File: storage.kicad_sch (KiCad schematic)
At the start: 26 parts, among them J11 uSD card, J9 uSD card, P1 uBUS1, P2 uBUS2, Q1 BC856, Q3 BC856, U19 IS61WV20488BLL-10TLI, U20 IS61WV20488BLL-10TLI, U21 MT48LC16M16A2TG

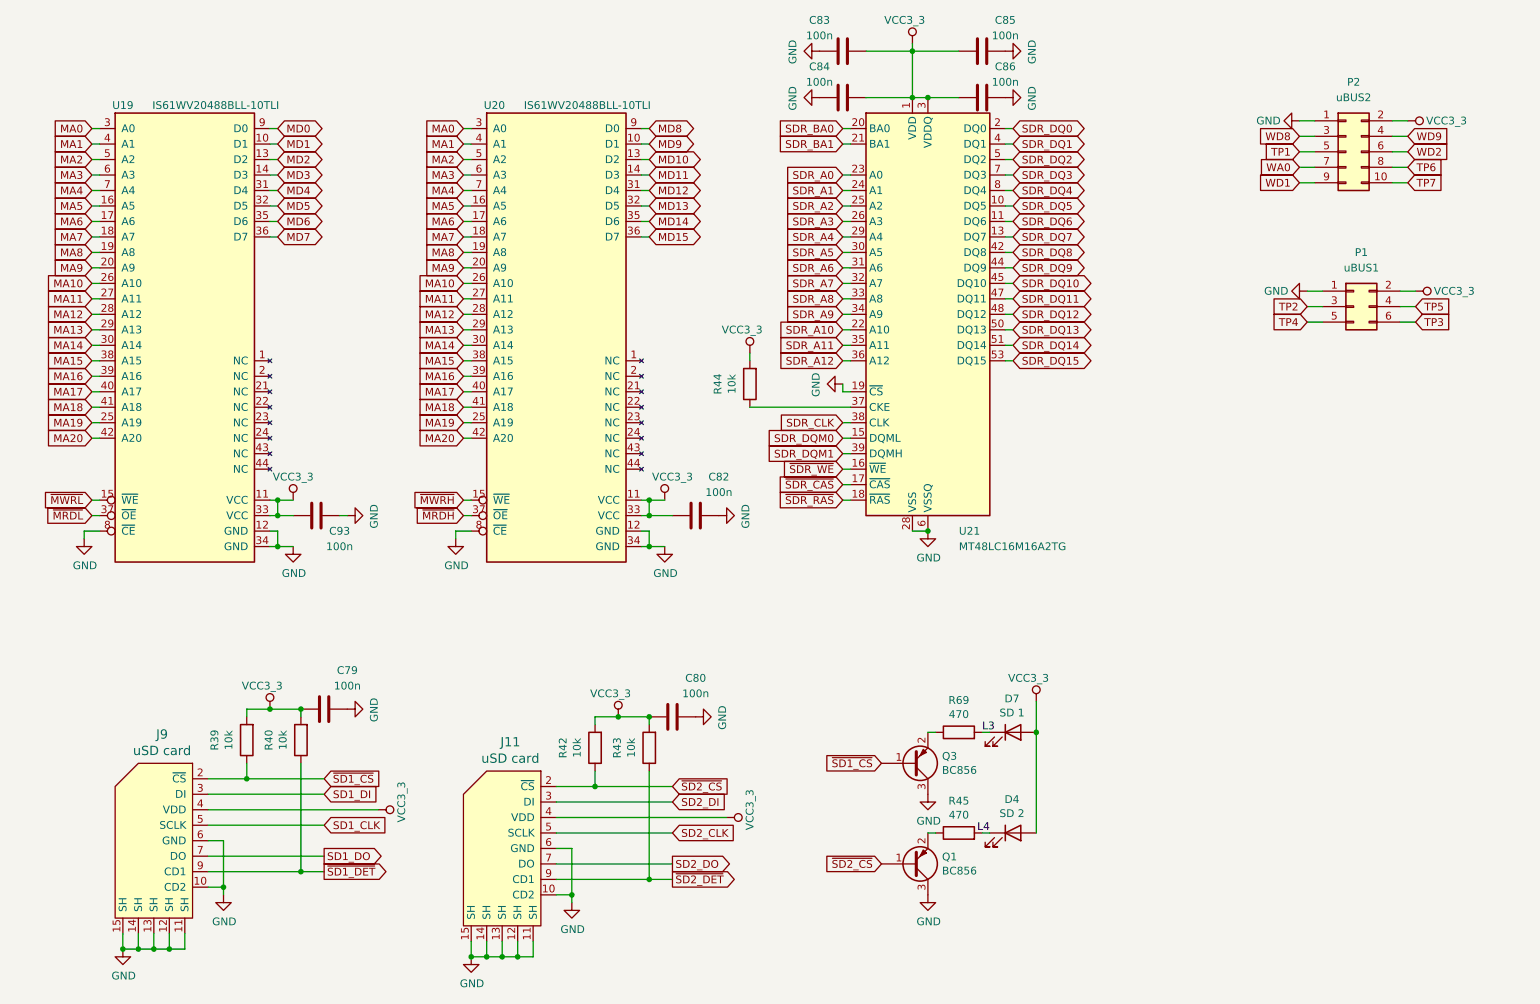
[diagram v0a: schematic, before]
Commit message: Updated revA: replaced resistors with IC for HDMI protection
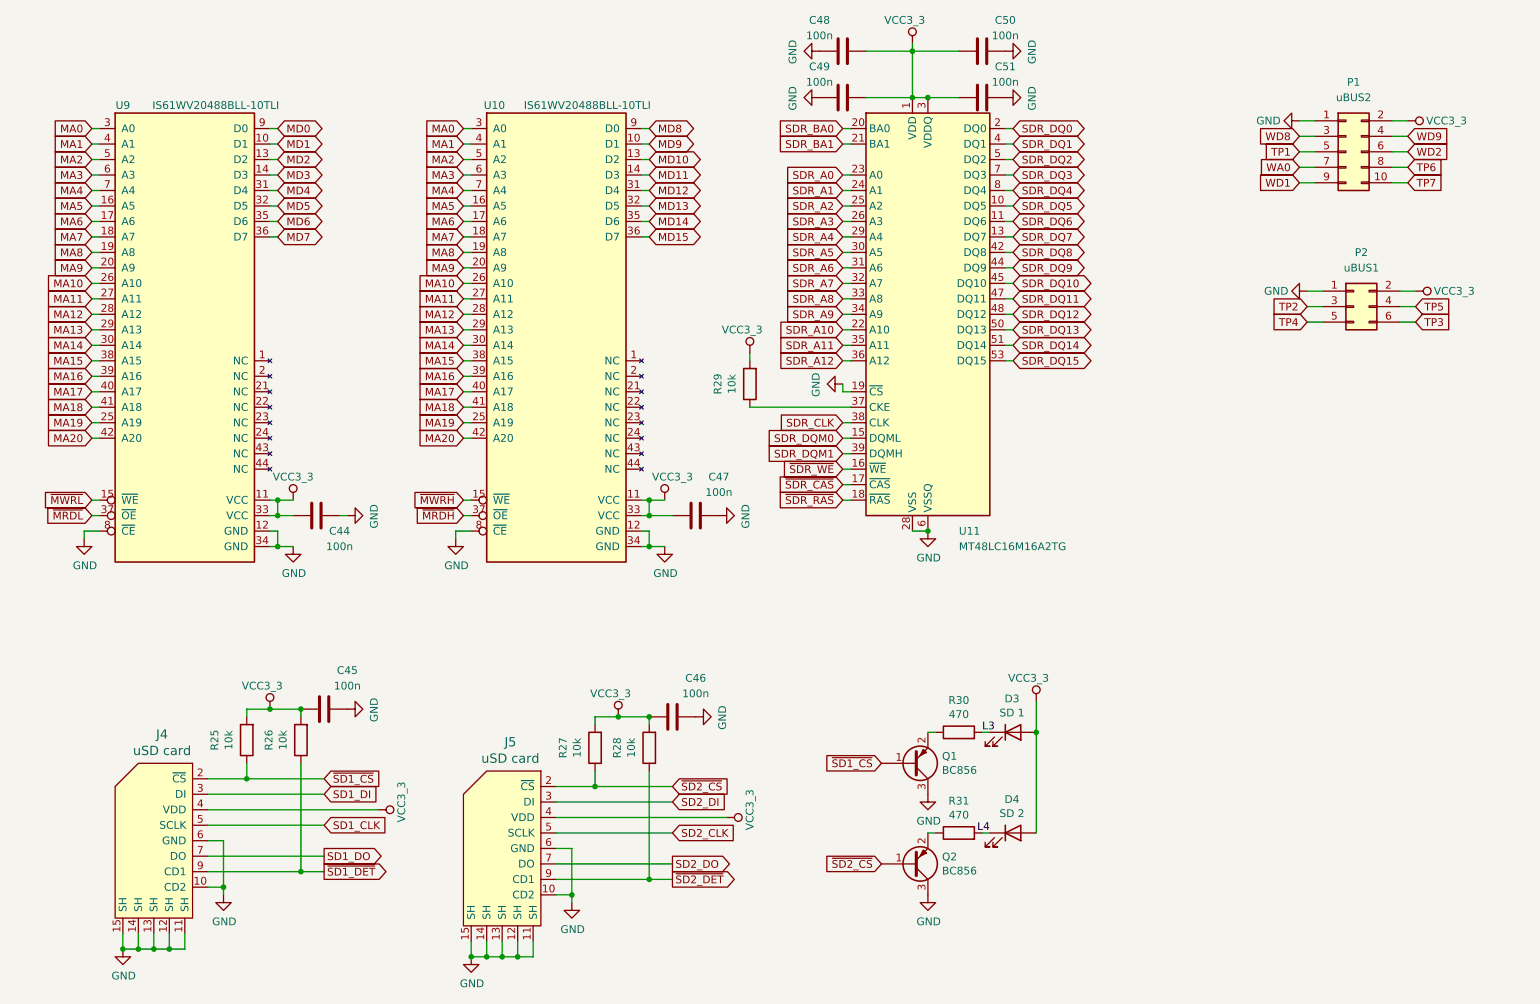
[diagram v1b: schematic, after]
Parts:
- renumbered C93 to C44, C79 to C45, C80 to C46, C82 to C47, C83 to C48, C84 to C49, C85 to C50, C86 to C51, D7 to D3, J9 to J4, J11 to J5, P2 to P1, P1 to P2, Q3 to Q1, Q1 to Q2, R39 to R25, R40 to R26, R42 to R27, R43 to R28, R44 to R29, R69 to R30, R45 to R31, U20 to U10, U21 to U11, U19 to U9

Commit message: Cleanup revA
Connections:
- net TP1 renamed UBUS_6
- net TP2 renamed UBUS_0
- net TP3 renamed UBUS_3
- net TP4 renamed UBUS_2
- net TP5 renamed UBUS_1
- net TP6 renamed UBUS_9
- net TP7 renamed UBUS_11
- net WA0 renamed UBUS_8
- net WD1 renamed UBUS_10
- net WD2 renamed UBUS_7
- net WD8 renamed UBUS_4
- net WD9 renamed UBUS_5
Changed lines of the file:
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@@
     (effects (font (size 1.27 1.27)) (justify left bottom))
   )
-  (global_label "TP7" (shape input) (at 242.57 44.45 0) (fields_autoplaced)
-    (effects (font (size 1.27 1.27)) (justify left))
-    (property "Intersheetrefs" "${INTERSHEET_REFS}" (at 249.0023 44.45 0)
+  (global_label "UBUS_11" (shape input) (at 242.57 44.45 0) (fields_autoplaced)
+    (effects (font (size 1.27 1.27)) (justify left))
+    (property "Intersheetrefs" "${INTERSHEET_REFS}" (at 254.0823 44.45 0)
       (effects (font (size 1.27 1.27)) (justify left) hide)
     )
@@
     )
   )
-  (global_label "TP4" (shape input) (at 226.06 67.31 180) (fields_autoplaced)
-    (effects (font (size 1.27 1.27)) (justify right))
-    (property "Intersheetrefs" "${INTERSHEET_REFS}" (at 219.6277 67.31 0)
+  (global_label "UBUS_2" (shape input) (at 226.06 67.31 180) (fields_autoplaced)
+    (effects (font (size 1.27 1.27)) (justify right))
+    (property "Intersheetrefs" "${INTERSHEET_REFS}" (at 215.7572 67.31 0)
       (effects (font (size 1.27 1.27)) (justify right) hide)
     )
@@
     )
   )
-  (global_label "TP2" (shape input) (at 226.06 64.77 180) (fields_autoplaced)
-    (effects (font (size 1.27 1.27)) (justify right))
-    (property "Intersheetrefs" "${INTERSHEET_REFS}" (at 219.6277 64.77 0)
+  (global_label "UBUS_0" (shape input) (at 226.06 64.77 180) (fields_autoplaced)
+    (effects (font (size 1.27 1.27)) (justify right))
+    (property "Intersheetrefs" "${INTERSHEET_REFS}" (at 215.7572 64.77 0)
       (effects (font (size 1.27 1.27)) (justify right) hide)
     )
@@
     )
   )
-  (global_label "TP1" (shape input) (at 224.79 39.37 180) (fields_autoplaced)
-    (effects (font (size 1.27 1.27)) (justify right))
-    (property "Intersheetrefs" "${INTERSHEET_REFS}" (at 218.3577 39.37 0)
-      (effects (font (size 1.27 1.27)) (justify right) hide)
-    )
-  )
-  (global_label "TP6" (shape input) (at 242.57 41.91 0) (fields_autoplaced)
-    (effects (font (size 1.27 1.27)) (justify left))
-    (property "Intersheetrefs" "${INTERSHEET_REFS}" (at 249.0023 41.91 0)
+  (global_label "UBUS_6" (shape input) (at 224.79 39.37 180) (fields_autoplaced)
+    (effects (font (size 1.27 1.27)) (justify right))
+    (property "Intersheetrefs" "${INTERSHEET_REFS}" (at 214.4872 39.37 0)
+      (effects (font (size 1.27 1.27)) (justify right) hide)
+    )
+  )
+  (global_label "UBUS_9" (shape input) (at 242.57 41.91 0) (fields_autoplaced)
+    (effects (font (size 1.27 1.27)) (justify left))
+    (property "Intersheetrefs" "${INTERSHEET_REFS}" (at 252.8728 41.91 0)
       (effects (font (size 1.27 1.27)) (justify left) hide)
     )
@@
     )
   )
-  (global_label "WD8" (shape input) (at 224.79 36.83 180) (fields_autoplaced)
-    (effects (font (size 1.27 1.27)) (justify right))
-    (property "Intersheetrefs" "${INTERSHEET_REFS}" (at 217.8739 36.83 0)
+  (global_label "UBUS_4" (shape input) (at 224.79 36.83 180) (fields_autoplaced)
+    (effects (font (size 1.27 1.27)) (justify right))
+    (property "Intersheetrefs" "${INTERSHEET_REFS}" (at 214.4872 36.83 0)
       (effects (font (size 1.27 1.27)) (justify right) hide)
     )
@@
     )
   )
-  (global_label "WD9" (shape input) (at 242.57 36.83 0) (fields_autoplaced)
-    (effects (font (size 1.27 1.27)) (justify left))
-    (property "Intersheetrefs" "${INTERSHEET_REFS}" (at 249.4861 36.83 0)
+  (global_label "UBUS_5" (shape input) (at 242.57 36.83 0) (fields_autoplaced)
+    (effects (font (size 1.27 1.27)) (justify left))
+    (property "Intersheetrefs" "${INTERSHEET_REFS}" (at 252.8728 36.83 0)
       (effects (font (size 1.27 1.27)) (justify left) hide)
     )
@@
     )
   )
-  (global_label "WD1" (shape input) (at 224.79 44.45 180) (fields_autoplaced)
-    (effects (font (size 1.27 1.27)) (justify right))
-    (property "Intersheetrefs" "${INTERSHEET_REFS}" (at 217.8739 44.45 0)
+  (global_label "UBUS_10" (shape input) (at 224.79 44.45 180) (fields_autoplaced)
+    (effects (font (size 1.27 1.27)) (justify right))
+    (property "Intersheetrefs" "${INTERSHEET_REFS}" (at 213.2777 44.45 0)
       (effects (font (size 1.27 1.27)) (justify right) hide)
     )
@@
     )
   )
-  (global_label "WA0" (shape input) (at 224.79 41.91 180) (fields_autoplaced)
-    (effects (font (size 1.27 1.27)) (justify right))
-    (property "Intersheetrefs" "${INTERSHEET_REFS}" (at 218.0553 41.91 0)
+  (global_label "UBUS_8" (shape input) (at 224.79 41.91 180) (fields_autoplaced)
+    (effects (font (size 1.27 1.27)) (justify right))
+    (property "Intersheetrefs" "${INTERSHEET_REFS}" (at 214.4872 41.91 0)
       (effects (font (size 1.27 1.27)) (justify right) hide)
     )
@@
     )
   )
-  (global_label "TP5" (shape input) (at 243.84 64.77 0) (fields_autoplaced)
-    (effects (font (size 1.27 1.27)) (justify left))
-    (property "Intersheetrefs" "${INTERSHEET_REFS}" (at 250.2723 64.77 0)
+  (global_label "UBUS_1" (shape input) (at 243.84 64.77 0) (fields_autoplaced)
+    (effects (font (size 1.27 1.27)) (justify left))
+    (property "Intersheetrefs" "${INTERSHEET_REFS}" (at 254.1428 64.77 0)
       (effects (font (size 1.27 1.27)) (justify left) hide)
     )
@@
     )
   )
-  (global_label "WD2" (shape input) (at 242.57 39.37 0) (fields_autoplaced)
-    (effects (font (size 1.27 1.27)) (justify left))
-    (property "Intersheetrefs" "${INTERSHEET_REFS}" (at 249.4861 39.37 0)
+  (global_label "UBUS_7" (shape input) (at 242.57 39.37 0) (fields_autoplaced)
+    (effects (font (size 1.27 1.27)) (justify left))
+    (property "Intersheetrefs" "${INTERSHEET_REFS}" (at 252.8728 39.37 0)
       (effects (font (size 1.27 1.27)) (justify left) hide)
     )
@@
     )
   )
-  (global_label "TP3" (shape input) (at 243.84 67.31 0) (fields_autoplaced)
-    (effects (font (size 1.27 1.27)) (justify left))
-    (property "Intersheetrefs" "${INTERSHEET_REFS}" (at 250.2723 67.31 0)
-      (effects (font (size 1.27 1.27)) (justify left) hide)
-    )
+  (global_label "UBUS_3" (shape input) (at 243.84 67.31 0) (fields_autoplaced)
+    (effects (font (size 1.27 1.27)) (justify left))
+    (property "Intersheetrefs" "${INTERSHEET_REFS}" (at 254.1428 67.31 0)
+      (effects (font (size 1.27 1.27)) (justify left) hide)
+    )

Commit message: Updated revB
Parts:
- added P3: uBUS3, Connector_PinHeader_1.27mm:PinHeader_2x07_P1.27mm_Vertical, symbol Connector_Generic:Conn_02x07_Odd_Even
- renumbered P2 to P1, P1 to P2
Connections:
- net GND: now also P3.1 (Pin_1)
- net VCC3_3: now also P3.2 (Pin_2)
- new net UBUS_12: P3.3 (Pin_3)
- new net UBUS_13: P3.4 (Pin_4)
- new net UBUS_14: P3.5 (Pin_5)
- new net UBUS_15: P3.6 (Pin_6)
- new net UBUS_16: P3.7 (Pin_7)
- new net UBUS_17: P3.8 (Pin_8)
- new net UBUS_18: P3.9 (Pin_9)
- new net UBUS_19: P3.10 (Pin_10)
- new net UBUS_20: P3.11 (Pin_11)
- new net UBUS_21: P3.12 (Pin_12)
- new net UBUS_22: P3.13 (Pin_13)
- new net UBUS_23: P3.14 (Pin_14)
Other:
- moved on the sheet: P2

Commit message: revG
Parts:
- P1: footprint Connector_PinHeader_1.27mm:PinHeader_2x03_P1.27mm_Vertical -> Connector_PinHeader_1.27mm:PinHeader_2x04_P1.27mm_Vertical; symbol Connector_Generic:Conn_02x03_Odd_Even -> Connector_Generic:Conn_02x04_Odd_Even
- P2: footprint Connector_PinHeader_1.27mm:PinHeader_2x05_P1.27mm_Vertical -> Connector_PinHeader_1.27mm:PinHeader_2x08_P1.27mm_Vertical; symbol Connector_Generic:Conn_02x05_Odd_Even -> Connector_Generic:Conn_02x08_Odd_Even
- P3: footprint Connector_PinHeader_1.27mm:PinHeader_2x07_P1.27mm_Vertical -> Connector_PinHeader_1.27mm:PinHeader_2x08_P1.27mm_Vertical; symbol Connector_Generic:Conn_02x07_Odd_Even -> Connector_Generic:Conn_02x08_Odd_Even
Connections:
- new net FT_GPIO0: P1.7 (Pin_7)
- new net FT_GPIO1: P1.8 (Pin_8)
- new net FT_SPI_MISO: P2.16 (Pin_16)
- new net FT_SPI_MOSI: P2.15 (Pin_15)
- new net FT_SPI_SCK: P2.14 (Pin_14)
- new net UBUS_24: P3.15 (Pin_15)
- new net UBUS_25: P3.16 (Pin_16)
- new net UBUS_26: P2.11 (Pin_11)
- new net UBUS_27: P2.12 (Pin_12)
- new net ~{FT_SPI_CS}: P2.13 (Pin_13)

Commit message: rev.G2 WIP
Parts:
- removed R29: 10k, Resistor_SMD:R_0603_1608Metric_Pad0.98x0.95mm_HandSolder, symbol Device:R
- added R20: 10k, Resistor_SMD:R_0603_1608Metric_Pad0.98x0.95mm_HandSolder, symbol Device:R
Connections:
- net GND: no longer U11.19 (~{CS})
- net VCC3_3: now also R20.2
- net at U11.37 (CKE): now also R20.1
- new net ~{SDR_CS}: U11.19 (~{CS})
